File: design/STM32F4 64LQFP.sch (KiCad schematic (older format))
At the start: 15 parts, among them P2 SWD, U1 STM32F40X_LQFP64, X2 8MHz 10ppm

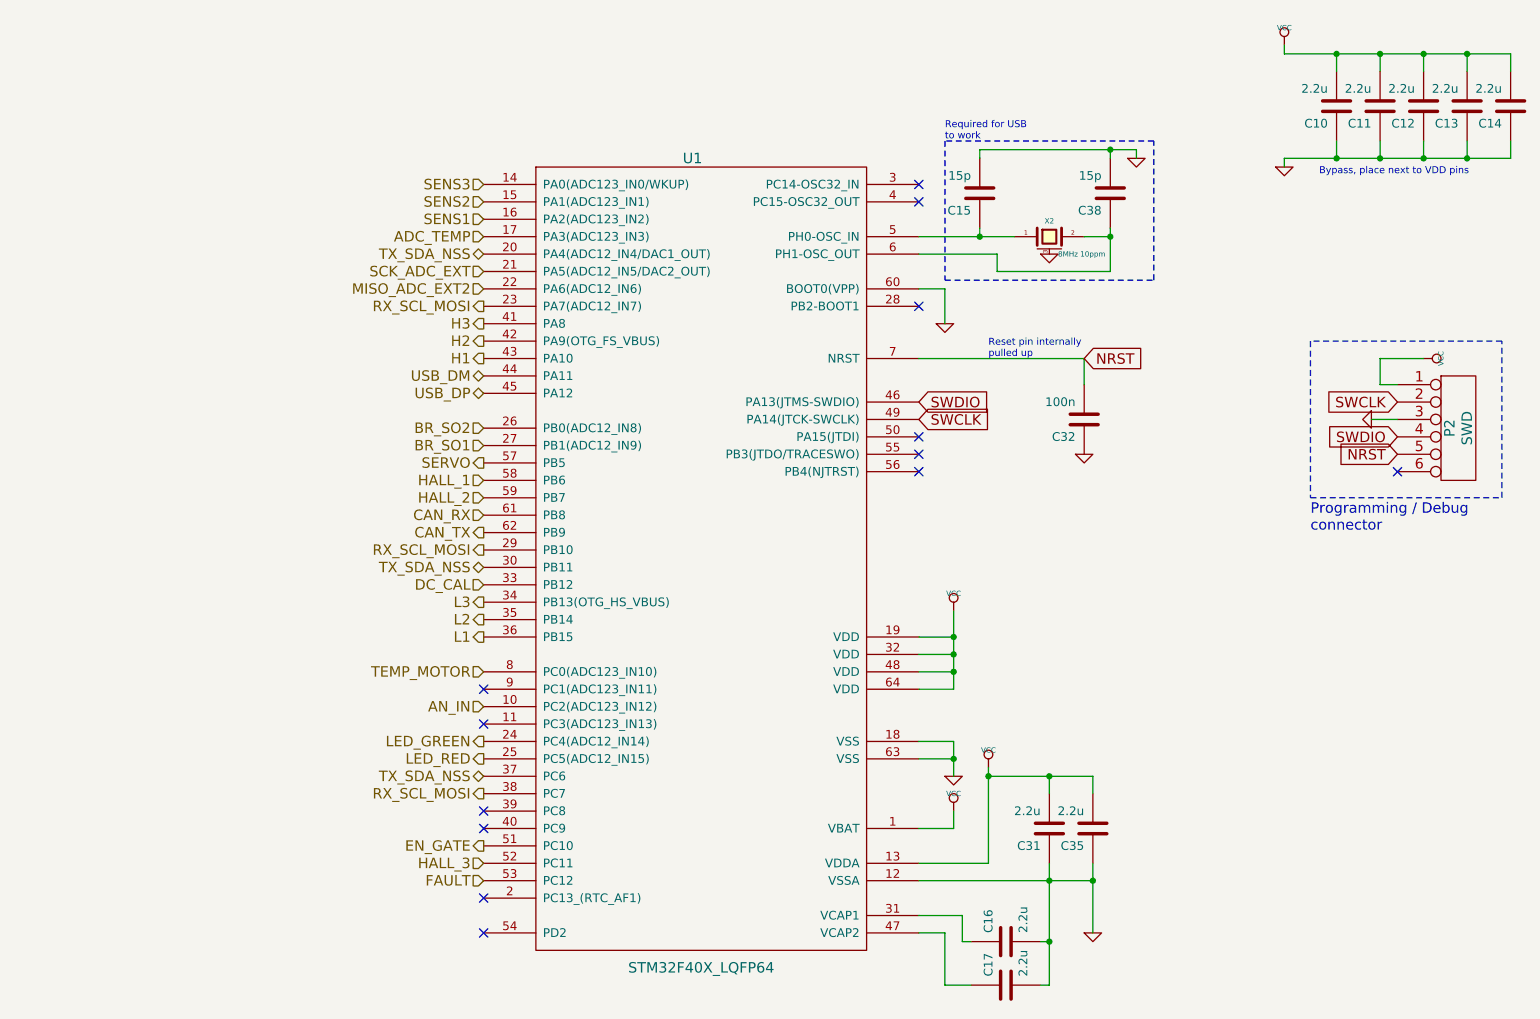
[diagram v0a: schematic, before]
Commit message: Implemented some improvements in schematic, but layout is completely new.
Changes in schematic:
- 3.3V or 5V CAN transceiver can be used
- DRV8301 can also be used and configured via SPI
- JTAG connector changed
- Fixed pinning of P1
- Some additional decoupling and/or filtering of analog signals
- Improved buck design according TI Webench recommendation
- Changed some component values
- maybe others...

Changes in layout:
- completely new layout
- placement of the big components is unchanged
- CAN connector rotated by 180°
- kept one layer free as a good GND plane
- many traces should be shorter and have lower impedance now
- improved buck layout

Other changes:
- updated gerber files
- updated PDFs (schematic and component placement)
- deleted all outdated files except libraries and datasheets
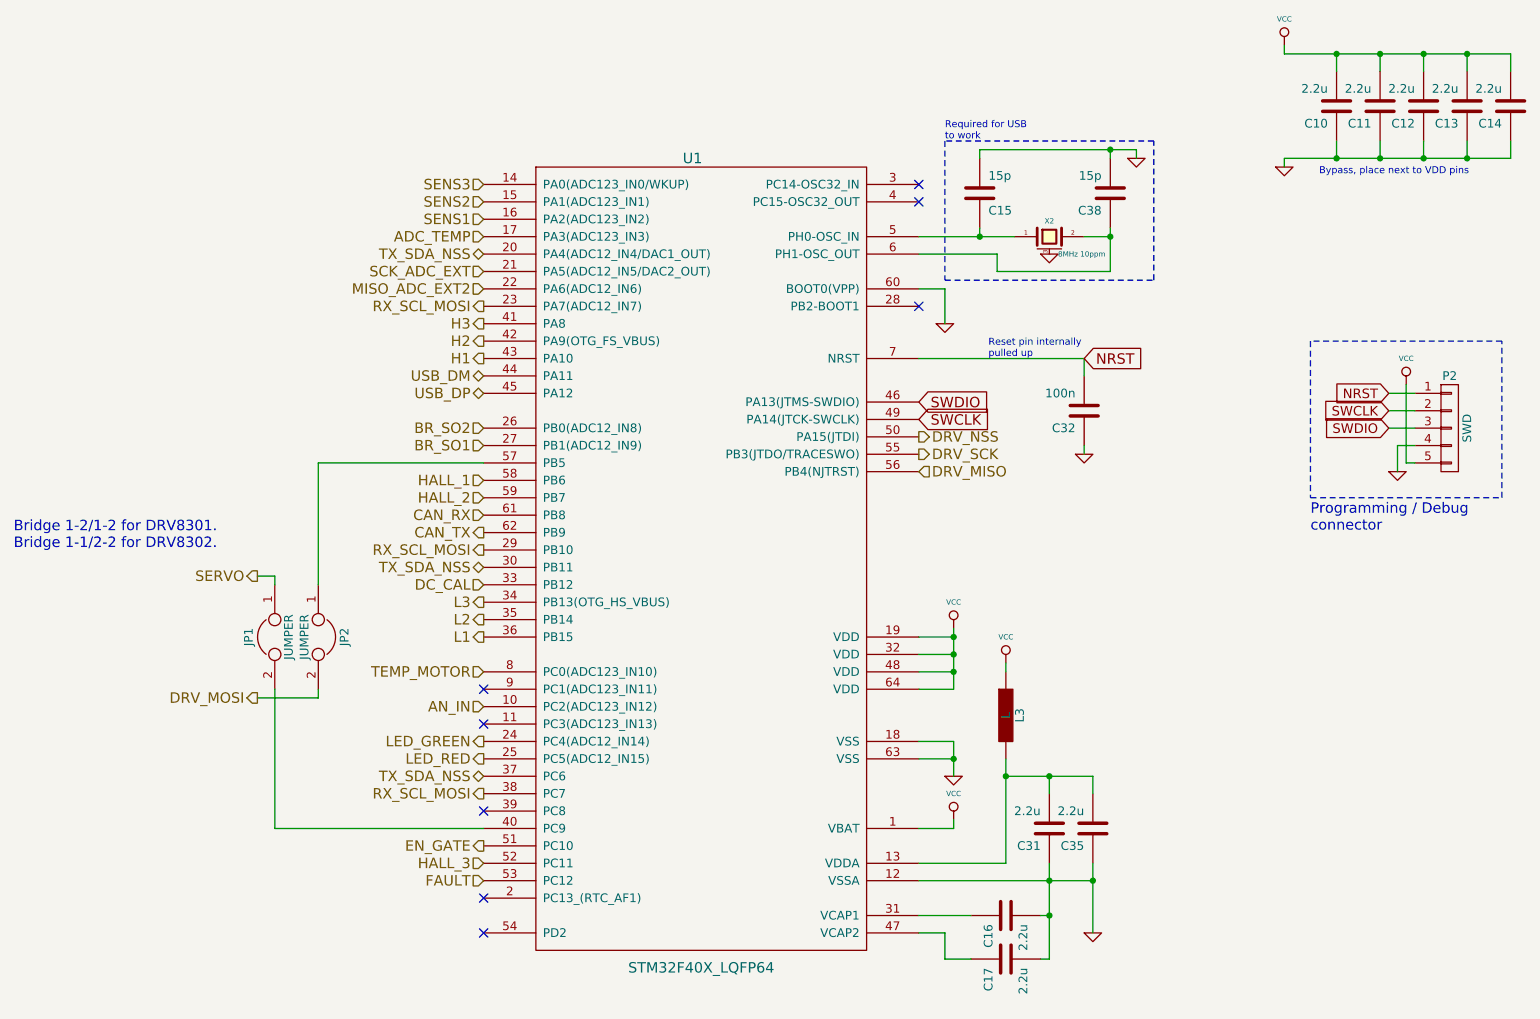
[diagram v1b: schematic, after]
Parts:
- removed P2: SWD, CRF1:MICRO_JST_6, symbol CONN_6
- added JP1, JP2: JUMPER, open-project:S_JUMPER_2, symbol JUMPER
- added L3: L, CRF1:SMD-0603_r, symbol L
- added P2: SWD, Pin_Headers:Pin_Header_Straight_1x05, symbol CONN_01X05
- C10, C11, C12, C13, C14, C16, C17, C31, C35: Part# (none) -> GRM188R61C225KAAD or GRM188C81A225KAAD
- X2: Part# (none) -> ABM3B-8.0-10-1UT; mfg# ABM3B-8.0-10-1UT -> (none)
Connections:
- net GND: now also P2.4 (P4)
- net NRST: now also P2.1 (P1)
- net SERVO: now also JP1.1; no longer U1.57 (PB5)
- net SWCLK: now also P2.2 (P2)
- net SWDIO: now also P2.3 (P3)
- net VCC: now also L3.1, P2.5 (P5); no longer C31.2, C35.2, U1.13 (VDDA)
- net at U1.40 (PC9): now also JP1.2
- net DRV_NSS: now reaches U1.50 (PA15(JTDI))
- net DRV_SCK: now reaches U1.55 (PB3(JTDO/TRACESWO))
- net DRV_MISO: now reaches U1.56 (PB4(NJTRST))
- new net: C31.2, C35.2, L3.2, U1.13 (VDDA)
- new net: JP2.1, U1.57 (PB5)
- new net DRV_MOSI: JP2.2
- no-connect marks 13 -> 8
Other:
- note added: "Bridge 1-2/1-2 for DRV8301.\nBridge 1-1/2-2 for DRV8302."
- moved on the sheet: C16, C17, C32
